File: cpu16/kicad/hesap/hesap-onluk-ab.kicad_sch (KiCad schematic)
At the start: 48 parts, among them U100 74HC32, U101 74HC32, U102 74HC32, U103 74HC283, U104 74HC283, U105 74HC283, U106 74HC283, U107 74HC283, U108 74HC283, U109 74HC283, U110 74HC08, U111 74HC08, U112 74HC32, U113 74HC32, U114 74HC32, U91 74HC283, U92 74HC283, U93 74HC283, U94 74HC283, U95 74HC283, U96 74HC283, U97 74HC283, U98 74HC08, U99 74HC08

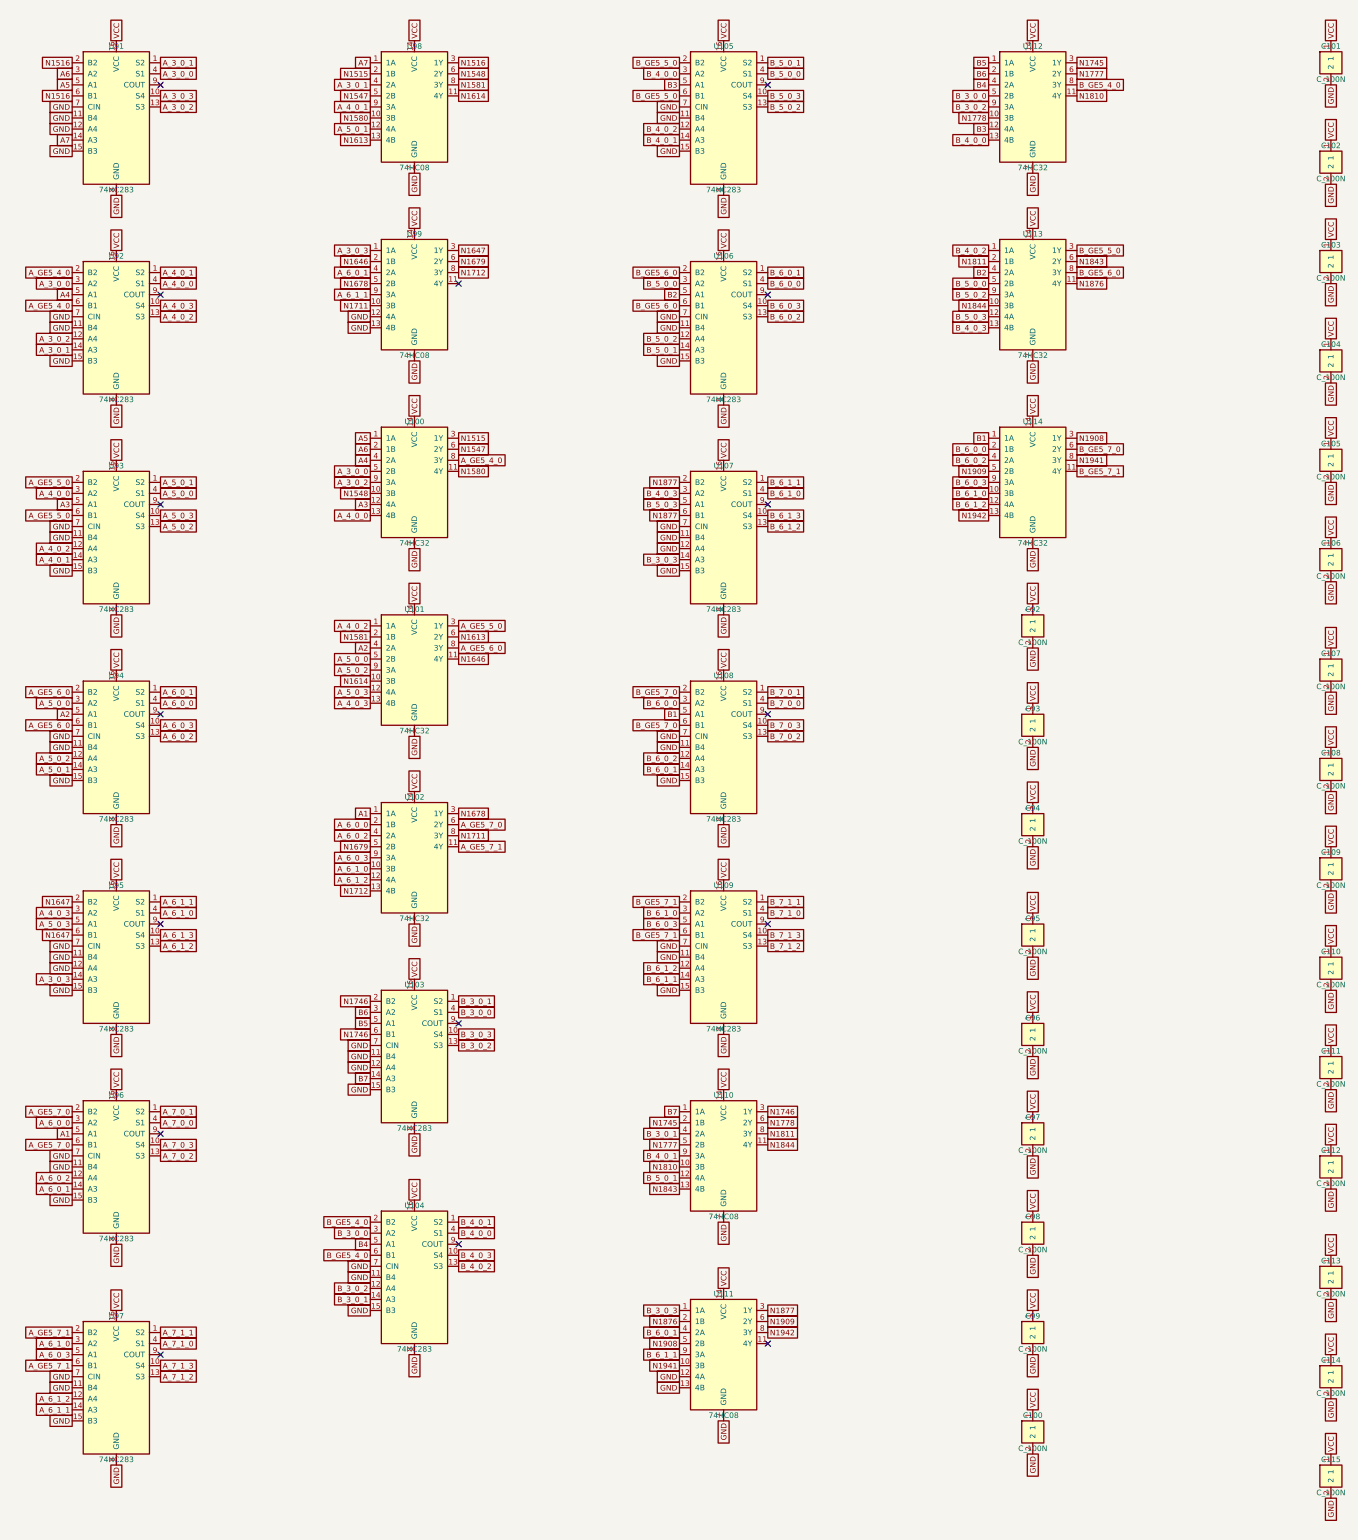
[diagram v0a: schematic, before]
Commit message: Hesap makinesi: eksi işareti sonucun solunda, lamba testinde de yanar; HATA LED'i göstergelerin yanında
- işaret hanesi (DS7) sonucun hanelerinden önce yerleşir: 3D kartta ve
  şemada en solda
- ISARET_g = NEG + lamba testi (boş kapı birimleriyle, çip sayısı aynı)
- HATA LED'i Bölme bloğundan "Gösterge: Sonuç" bloğuna
- rehber ve tasarım belgesi güncellendi

Co-Authored-By: Claude Opus 5.5 (1M context) <noreply@anthropic.com>
Claude-Session: https://claude.ai/code/session_018J8WVuECVRbQJyCbmF6Nsi
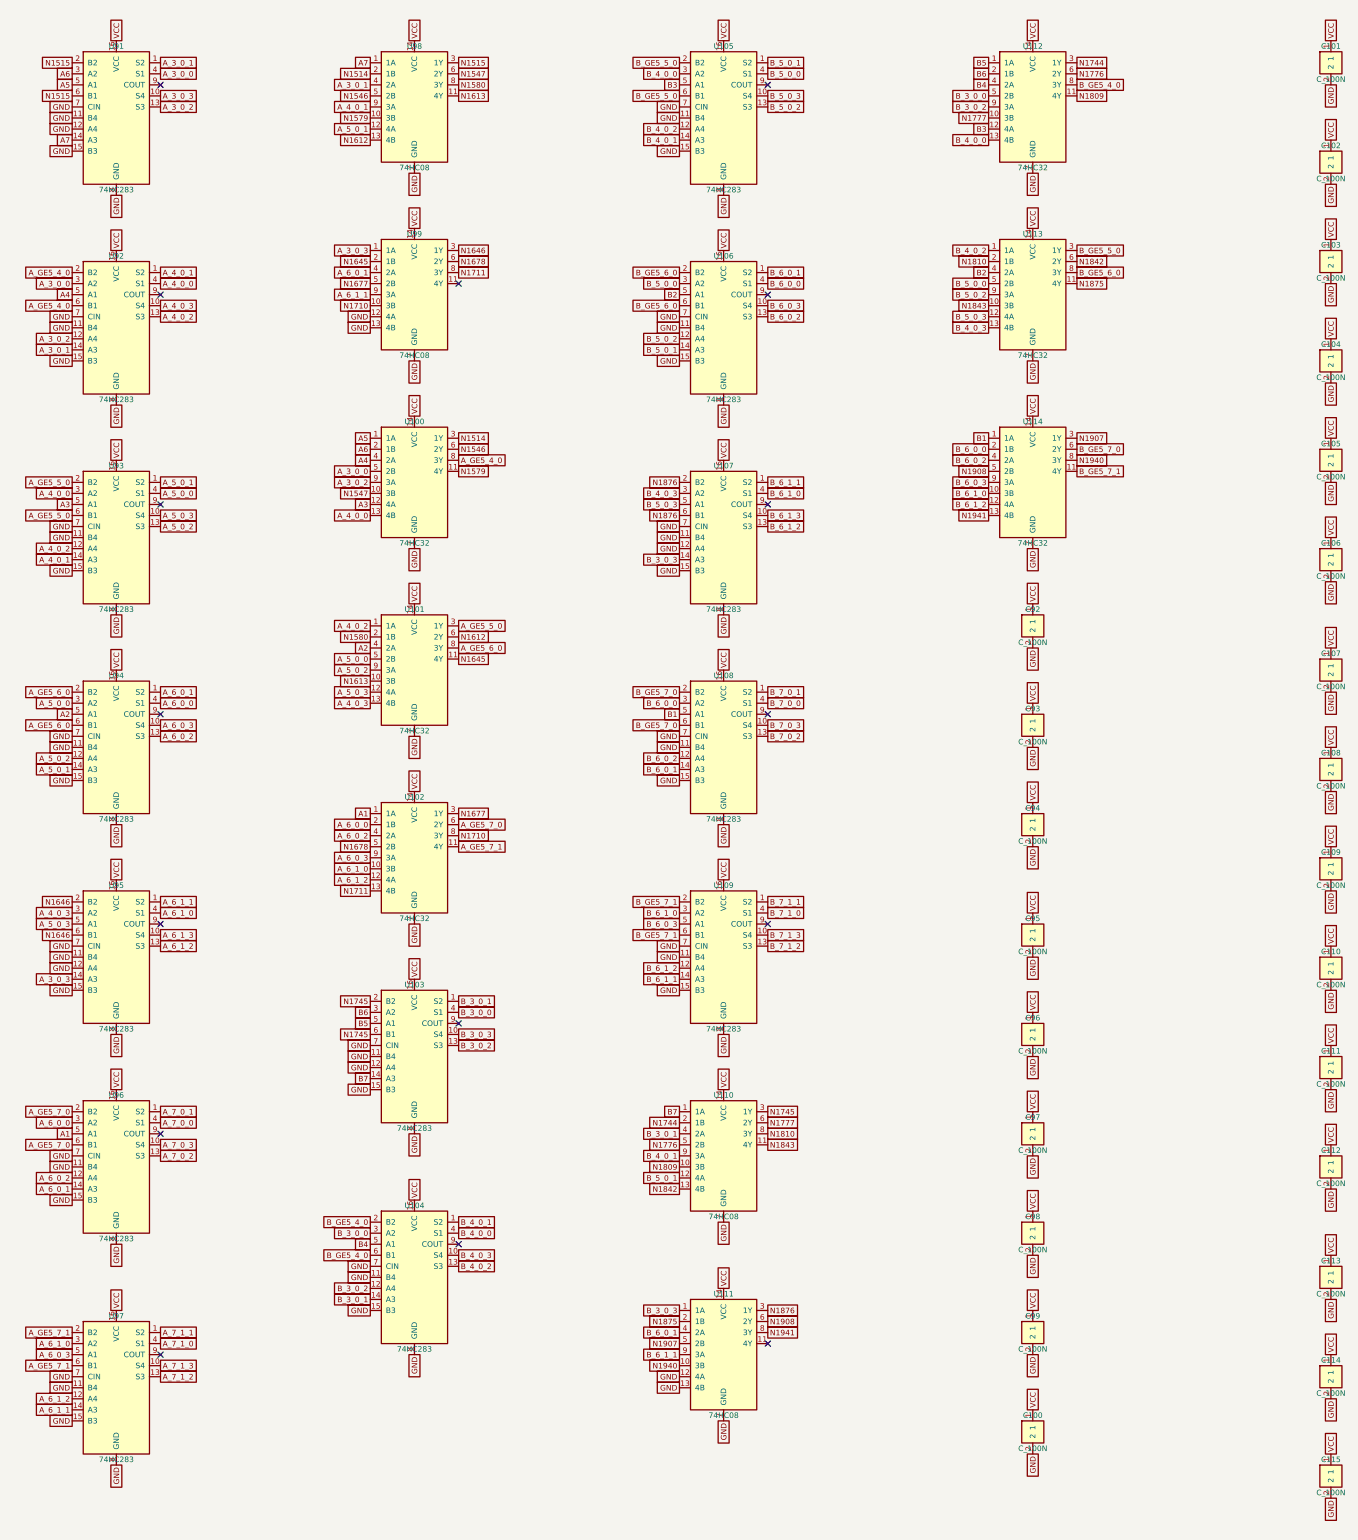
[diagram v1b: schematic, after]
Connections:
- net N1516 is gone; now on net N1515: U91.2 (B2), U91.6 (B1), U98.3 (1Y)
- net N1548 is gone; now on net N1547: U100.10 (3B), U98.6 (2Y)
- net N1581 is gone; now on net N1580: U101.2 (1B), U98.8 (3Y)
- net N1614 is gone; now on net N1613: U101.10 (3B), U98.11 (4Y)
- net N1647 is gone; now on net N1646: U95.2 (B2), U95.6 (B1), U99.3 (1Y)
- net N1679 is gone; now on net N1678: U102.5 (2B), U99.6 (2Y)
- net N1712 is gone; now on net N1711: U102.13 (4B), U99.8 (3Y)
- net N1746 is gone; now on net N1745: U103.2 (B2), U103.6 (B1), U110.3 (1Y)
- net N1778 is gone; now on net N1777: U110.6 (2Y), U112.10 (3B)
- net N1811 is gone; now on net N1810: U110.8 (3Y), U113.2 (1B)
- net N1844 is gone; now on net N1843: U110.11 (4Y), U113.10 (3B)
- net N1877 is gone; now on net N1876: U107.2 (B2), U107.6 (B1), U111.3 (1Y)
- net N1909 is gone; now on net N1908: U111.6 (2Y), U114.5 (2B)
- net N1942 is gone; now on net N1941: U111.8 (3Y), U114.13 (4B)
- net N1515: no longer U100.3 (1Y), U98.2 (1B)
- net N1547: no longer U100.6 (2Y), U98.5 (2B)
- net N1580: no longer U100.11 (4Y), U98.10 (3B)
- net N1613: no longer U101.6 (2Y), U98.13 (4B)
- net N1646: no longer U101.11 (4Y), U99.2 (1B)
- net N1678: no longer U102.3 (1Y), U99.5 (2B)
- net N1711: no longer U102.8 (3Y), U99.10 (3B)
- net N1745: no longer U110.2 (1B), U112.3 (1Y)
- net N1777: no longer U110.5 (2B), U112.6 (2Y)
- net N1810: no longer U110.10 (3B), U112.11 (4Y)
- net N1843: no longer U110.13 (4B), U113.6 (2Y)
- net N1876: no longer U111.2 (1B), U113.11 (4Y)
- net N1908: no longer U111.5 (2B), U114.3 (1Y)
- net N1941: no longer U111.10 (3B), U114.8 (3Y)
- new net N1514: U100.3 (1Y), U98.2 (1B)
- new net N1546: U100.6 (2Y), U98.5 (2B)
- new net N1579: U100.11 (4Y), U98.10 (3B)
- new net N1612: U101.6 (2Y), U98.13 (4B)
- new net N1645: U101.11 (4Y), U99.2 (1B)
- new net N1677: U102.3 (1Y), U99.5 (2B)
- new net N1710: U102.8 (3Y), U99.10 (3B)
- new net N1744: U110.2 (1B), U112.3 (1Y)
- new net N1776: U110.5 (2B), U112.6 (2Y)
- new net N1809: U110.10 (3B), U112.11 (4Y)
- new net N1842: U110.13 (4B), U113.6 (2Y)
- new net N1875: U111.2 (1B), U113.11 (4Y)
- new net N1907: U111.5 (2B), U114.3 (1Y)
- new net N1940: U111.10 (3B), U114.8 (3Y)
